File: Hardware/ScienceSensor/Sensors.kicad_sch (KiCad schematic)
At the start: 0 parts

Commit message: Created NO sensor, NH3 sensor, worked on Mosfets, and created Methane sensor with labels.
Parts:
- added Blue: D13, symbol Device:LED
- added Blue: D11, symbol Device:LED
- added Blue: D12, symbol Device:LED
- added Blue: D10, symbol Device:LED
- added Conn4, Conn5: Molex_SL_04, symbol MRDT_Connectors:Molex_SL_04
- added R10, R11, R12, R13: 480, symbol Device:R
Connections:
- new net: Blue.2 (A), R13.1
- new net: Blue.2 (A), R11.1
- new net: Blue.2 (A), R12.1
- new net: Blue.2 (A), R10.1
- new net +5V: Conn4.1, Conn5.1
- new net CO2_RX: Conn4.4, R11.2
- new net CO2_TX: Conn4.3, R10.2
- new net GND: Blue.1 (K), Blue.1 (K), Blue.1 (K), Blue.1 (K), Conn4.2, Conn5.2
- new net O2_RX: Conn5.4, R13.2
- new net O2_TX: Conn5.3, R12.2
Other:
- note added: "CO2_Sensor"
- note added: "O2_Sensor"

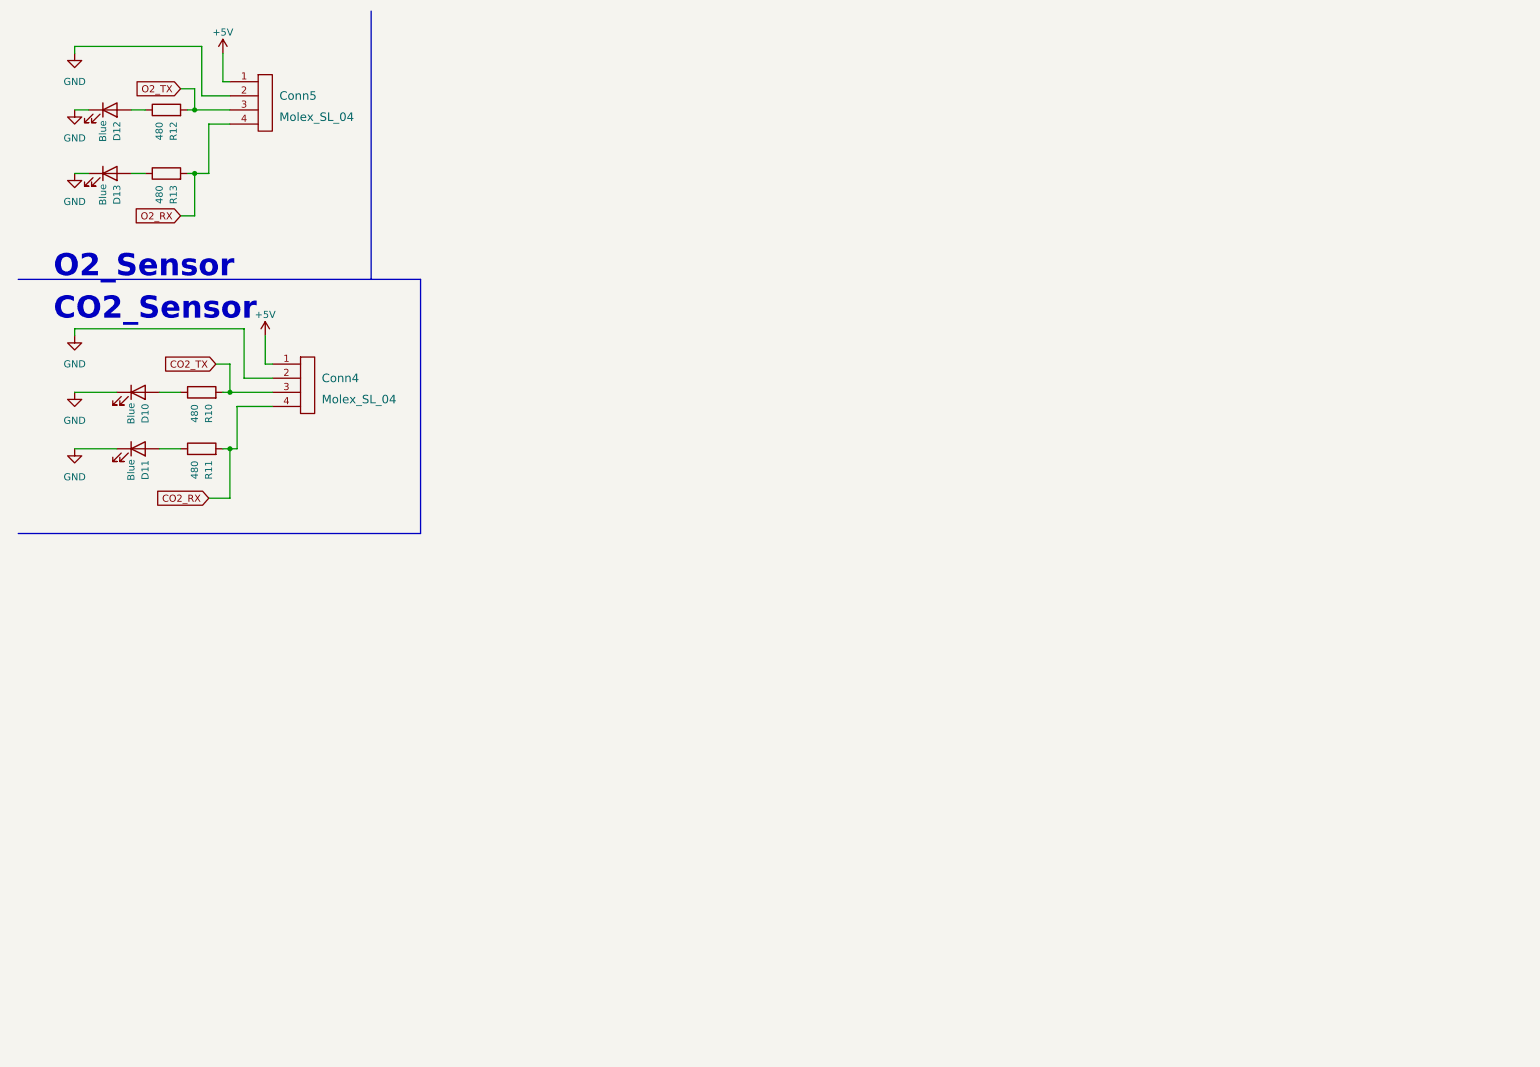
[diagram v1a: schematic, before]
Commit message: Finished mosfets.
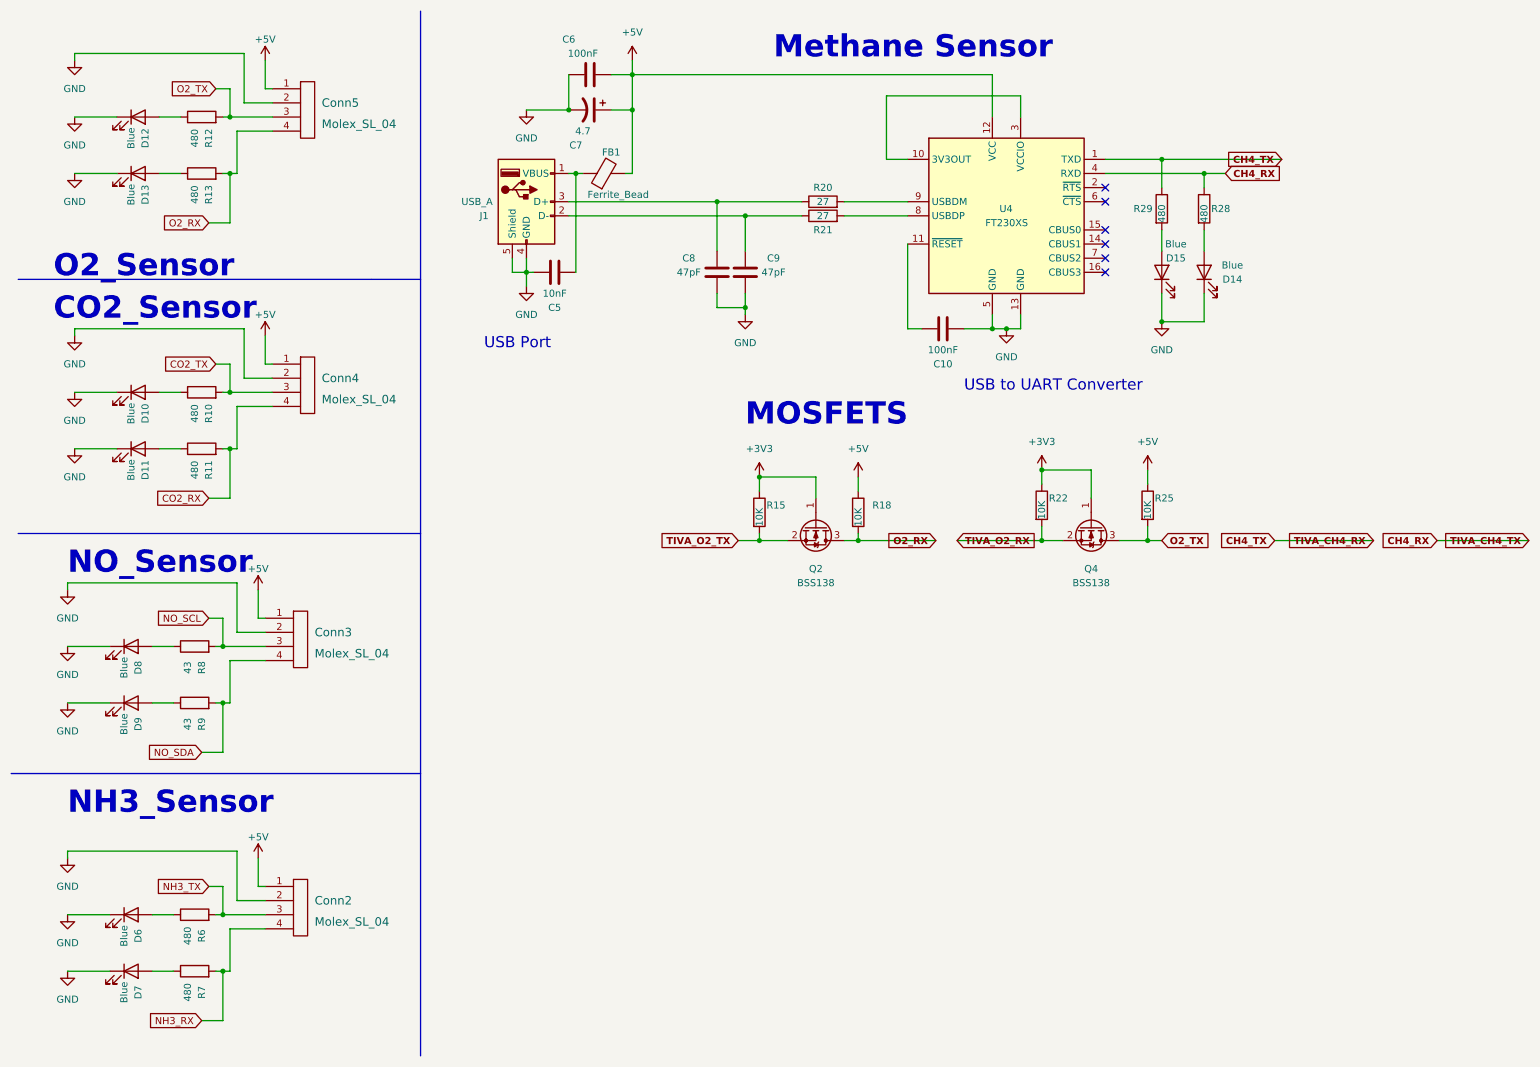
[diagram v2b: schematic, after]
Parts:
- removed Blue: D13, symbol Device:LED
- removed Blue: D12, symbol Device:LED
- added Blue: D9, symbol Device:LED
- added Blue: D14, symbol Device:LED
- added Blue: D6, symbol Device:LED
- added Blue: D8, symbol Device:LED
- added Blue: D12, symbol Device:LED
- added Blue: D13, symbol Device:LED
- added Blue: D15, symbol Device:LED
- added Blue: D7, symbol Device:LED
- added C10, C6: 100nF, symbol Device:C
- added C5: 10nF, symbol Device:C
- added C7: 4.7, symbol Device:C_Polarized_US
- added C8, C9: 47pF, symbol Device:C
- added Conn2, Conn3: Molex_SL_04, symbol MRDT_Connectors:Molex_SL_04
- added FB1: Ferrite_Bead, symbol Device:FerriteBead
- added J1: USB_A, symbol Connector:USB_A
- added Q2, Q4: BSS138, symbol Device:Q_NMOS_GSD
- added R15, R18, R22, R25: 10K, symbol Device:R
- added R20, R21: 27, symbol Device:R
- added R28, R29, R6, R7: 480, symbol Device:R
- added R8, R9: 43, symbol Device:R
- added U4: FT230XS, Package_SO:SSOP-16_3.9x4.9mm_P0.635mm, symbol Interface_USB:FT230XS
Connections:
- net +5V: now also C6.2, C7.1, Conn2.1, Conn3.1, FB1.2, R18.1, R25.1, U4.12 (VCC)
- net GND: now also Blue.1 (K), Blue.1 (K), Blue.1 (K), Blue.1 (K), Blue.1 (K), Blue.1 (K), Blue.1 (K), Blue.1 (K), C10.2, C5.1, C6.1, C7.2, C8.1, C9.1, Conn2.2, Conn3.2, J1.4 (GND), J1.5 (Shield), U4.13 (GND), U4.5 (GND)
- net O2_RX: now also Q2.3 (D), R18.2
- net O2_TX: now also Q4.3 (D), R25.2
- net at R13.1: now also Blue.2 (A)
- net at R12.1: now also Blue.2 (A)
- new net: Blue.2 (A), R7.1
- new net: C5.2, FB1.1, J1.1 (VBUS)
- new net: C9.2, J1.2 (D-), R21.1
- new net: C8.2, J1.3 (D+), R20.1
- new net: Blue.2 (A), R9.1
- new net: C10.1, U4.11 (~{RESET})
- new net: Blue.2 (A), R29.2
- new net: Blue.2 (A), R28.2
- new net: R20.2, U4.9 (USBDM)
- new net: Blue.2 (A), R8.1
- new net: Blue.2 (A), R6.1
- new net: U4.10 (3V3OUT), U4.3 (VCCIO)
- new net: R21.2, U4.8 (USBDP)
- new net +3V3: Q2.1 (G), Q4.1 (G), R15.1, R22.1
- new net CH4_RX: R28.1, U4.4 (RXD)
- new net CH4_TX: R29.1, U4.1 (TXD)
- new net NH3_RX: Conn2.4, R7.2
- new net NH3_TX: Conn2.3, R6.2
- new net NO_SCL: Conn3.3, R8.2
- new net NO_SDA: Conn3.4, R9.2
- new net TIVA_O2_RX: Q4.2 (S), R22.2
- new net TIVA_O2_TX: Q2.2 (S), R15.2
- no-connect marks 0 -> 6
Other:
- note added: "MOSFETS"
- note added: "Methane Sensor"
- note added: "NH3_Sensor"
- note added: "NO_Sensor"
- note added: "USB Port"
- note added: "USB to UART Converter"

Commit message: BOM generated, photodiodes added
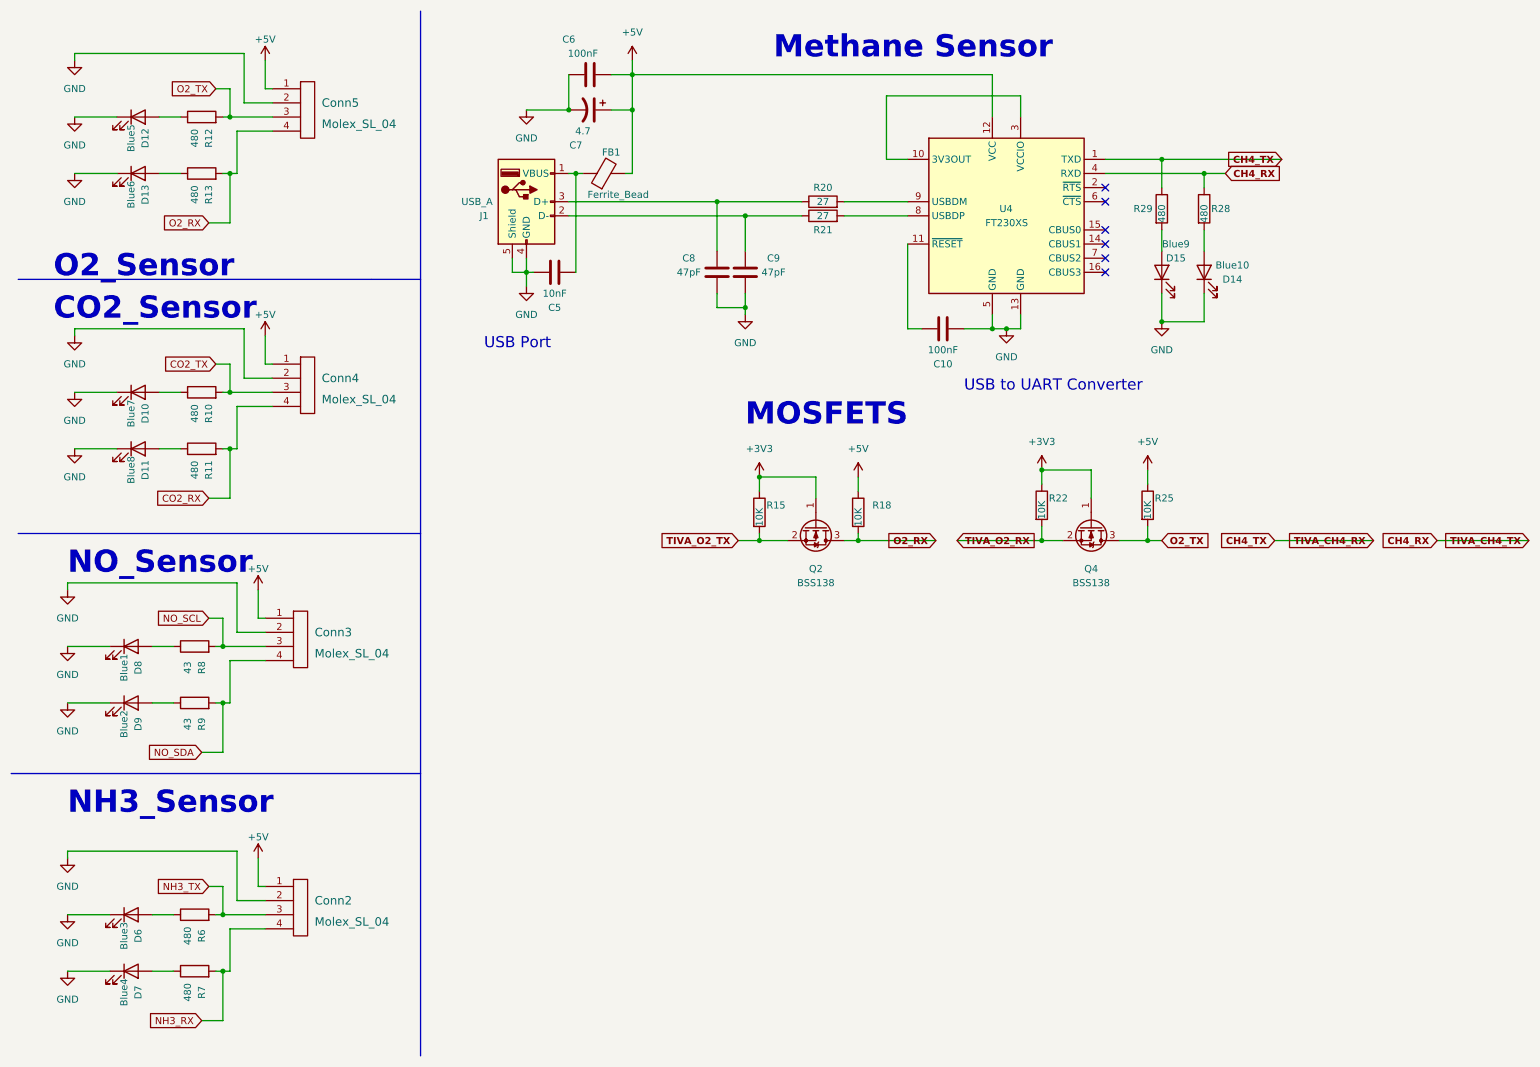
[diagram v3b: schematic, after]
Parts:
- renumbered Blue to Blue1, Blue to Blue10, Blue to Blue2, Blue to Blue3, Blue to Blue4, Blue to Blue5, Blue to Blue6, Blue to Blue7, Blue to Blue8, Blue to Blue9
